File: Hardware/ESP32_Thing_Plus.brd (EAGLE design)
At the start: 22.9 x 58.4 mm, 104 parts, among them Q1 2.5A/30V, Q2 MBT3904DW1T1, U1 MCP73831, U2 ESP-WROOM-32NARROW, U3 AP2112K-3.3V, U4 CP2102N

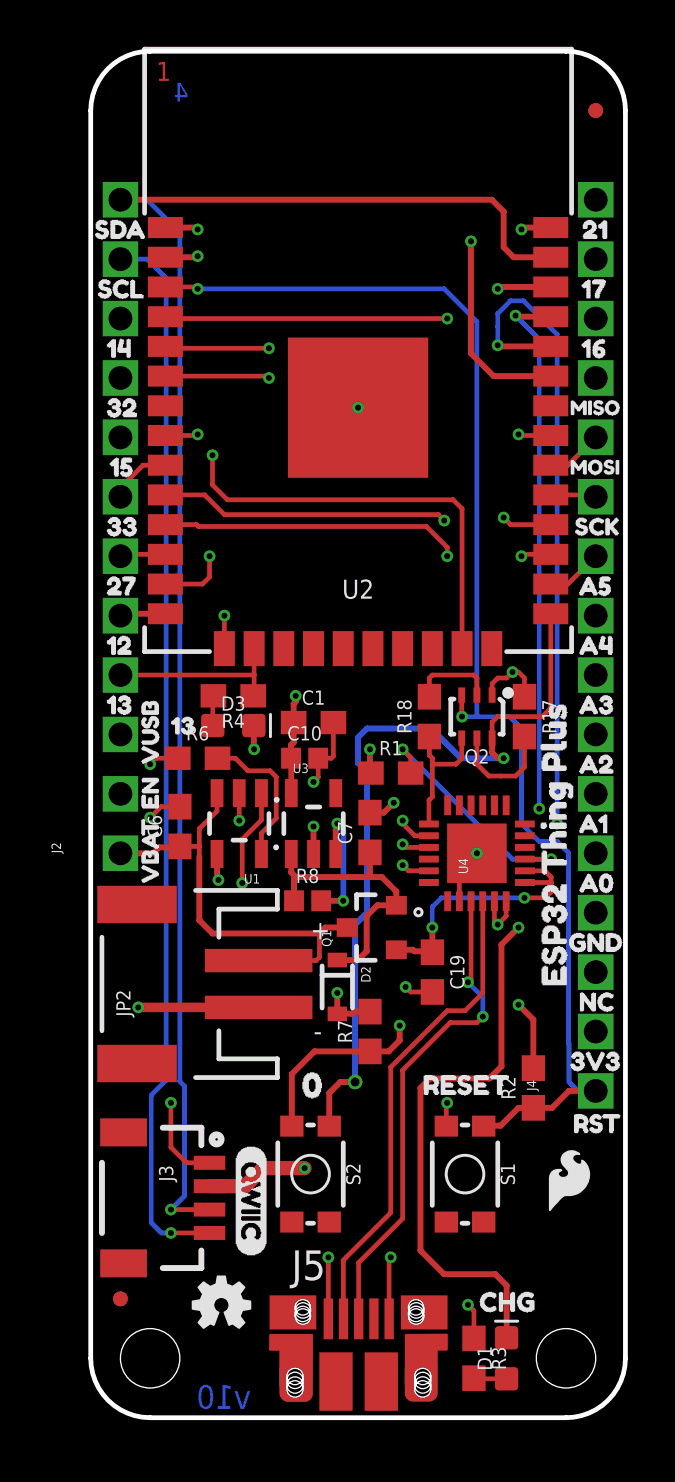
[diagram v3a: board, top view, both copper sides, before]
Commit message: v10 design review changes
- Moved battery connector away from headers by 0.030"
- Moved charge led and resistor away from standoff
- Fixed silk on header pins 21 and 12
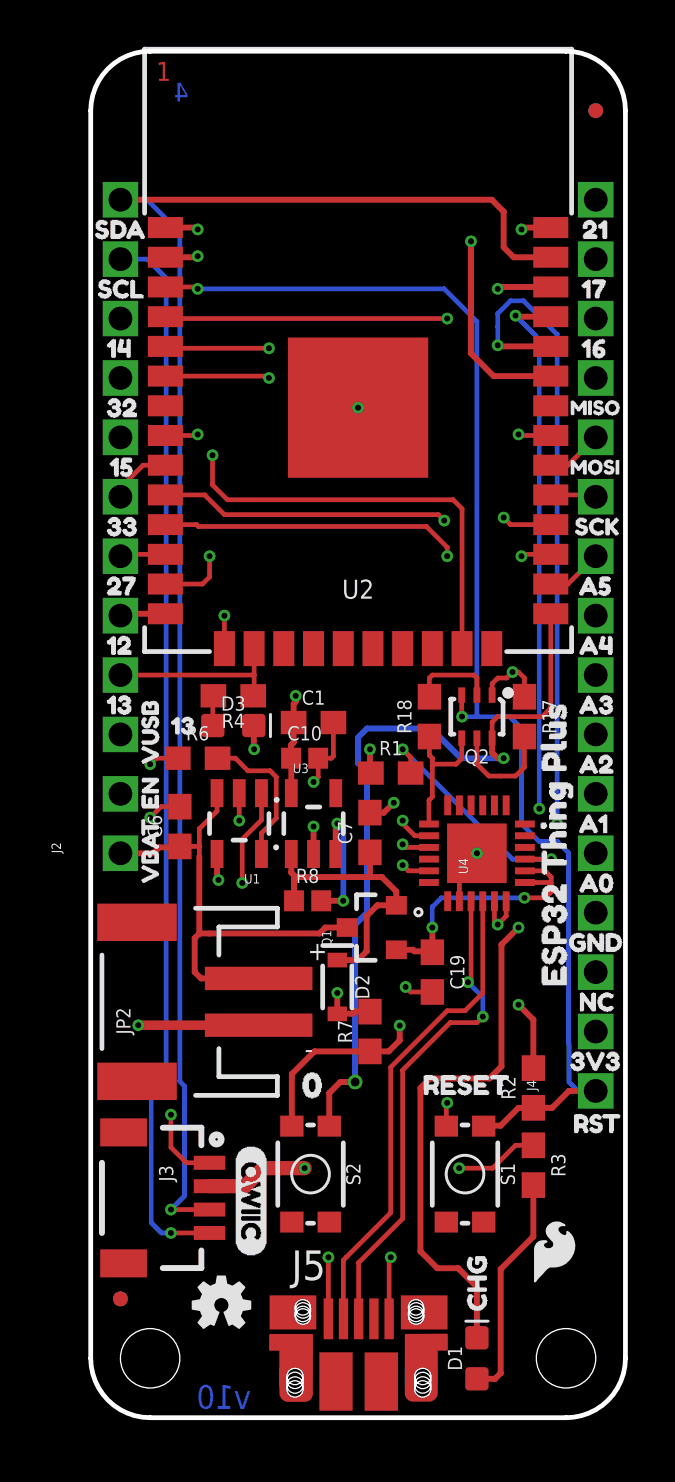
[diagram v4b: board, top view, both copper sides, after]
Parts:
- D2: value BAT20J -> 1A/23V/620mV
- Q1: device SparkFun-DiscreteSemi:SOT23-3 -> SparkFun-DiscreteSemi:SOT23-3@1
- U$8: device buzzard_labels (37):2022 -> buzzard_labels (8):121
- U$9: device buzzard_labels (37):2314 -> buzzard_labels (8):210
- moved R3 8.64 mm to (18.9, 10.8)
- moved LOGO1 3.11 mm to (18.7, 5.46)
- moved U$56 1.31 mm to (16.5, 3.81), turned to 90 degrees
- moved D1 1.27 mm to (16.5, 2.54)
- moved JP2 0.76 mm to (3.48, 17.8)
- moved U$8 0.28 mm to (4.93, 34.3)
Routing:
- net N$17: track 1.45 -> 9.74 mm
- net V_USB: track 19.5 -> 21.6 mm
- net CHG: track 41.7 -> 40.4 mm
- net V_BATT: track 19.6 -> 20.8 mm
- net GND: track 39.0 -> 38.5 mm

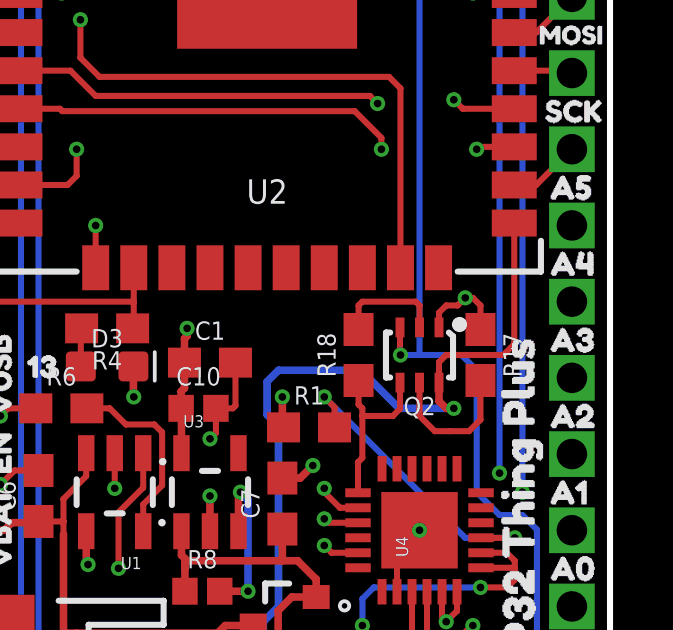
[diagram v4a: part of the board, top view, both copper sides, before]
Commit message: v10 design review changes cont.
Fixed pin 1 marker on dual NPN transistor
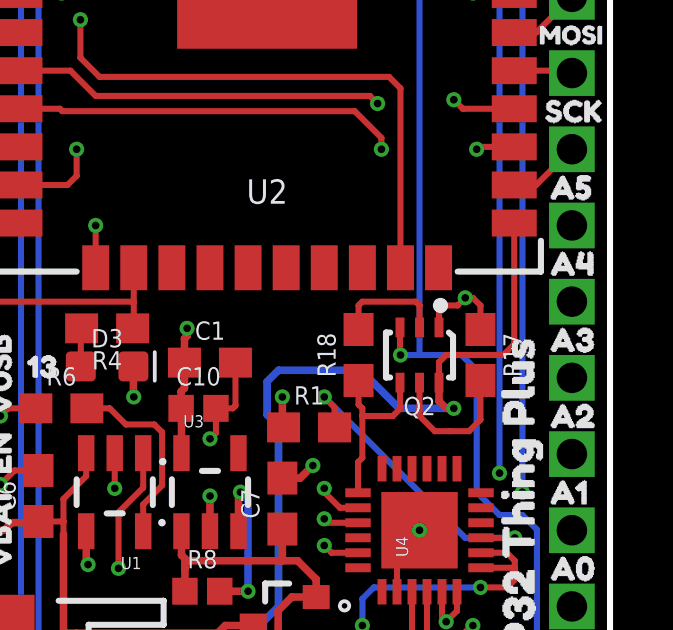
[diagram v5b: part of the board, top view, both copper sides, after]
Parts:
- Q2: device esp32-thing-temp:SC70-6 -> SparkFun-DiscreteSemi:SC70-6
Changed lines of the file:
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@@
 <attribute name="PROD_ID" value="RES-00824" x="8.128" y="18.542" size="1.778" layer="27" font="vector" ratio="15" rot="R90" display="off"/>
 </element>
-<element name="Q2" library="esp32-thing-temp" package="SC70-6" value="MBT3904DW1T1" x="16.51" y="29.972" rot="R180">
+<element name="Q2" library="SparkFun-DiscreteSemi" package="SC70-6" value="MBT3904DW1T1" x="16.51" y="29.972" rot="R180">
 <attribute name="PROD_ID" value="TRANS-13337" x="16.51" y="29.972" size="1.778" layer="27" rot="R180" display="off"/>
 </element>

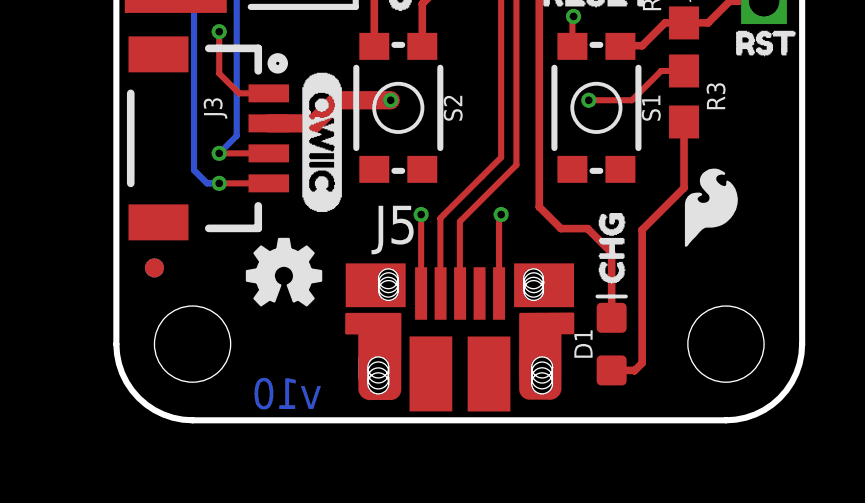
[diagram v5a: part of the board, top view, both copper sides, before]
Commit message: v10 QC Fixes
- Replaced drill hit with standoff
- Added VCC range and battery type to schematic
- Updated USB connector
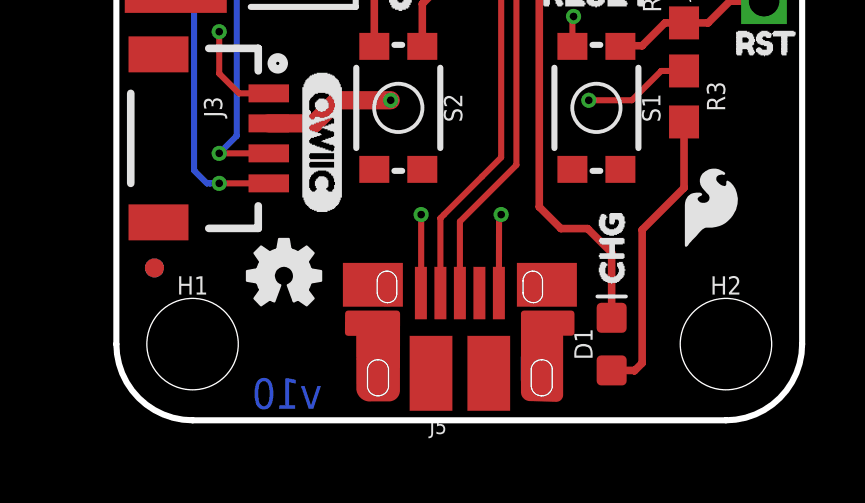
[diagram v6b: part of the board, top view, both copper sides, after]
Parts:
- added H1, H2: STAND-OFFTIGHT, SparkFun-Hardware:STAND-OFF-TIGHT
- J5: device SparkFun-Connectors:USB-MICROB-PTH -> SparkFun-Connectors:USB-MICROB-PTH-MILL
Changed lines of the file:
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@@
 <layer number="27" name="tValues" color="7" fill="1" visible="no" active="yes"/>
 <layer number="28" name="bValues" color="7" fill="1" visible="no" active="yes"/>
-<layer number="29" name="tStop" color="7" fill="3" visible="yes" active="yes"/>
+<layer number="29" name="tStop" color="7" fill="3" visible="no" active="yes"/>
 <layer number="30" name="bStop" color="7" fill="6" visible="no" active="yes"/>
 <layer number="31" name="tCream" color="7" fill="4" visible="no" active="yes"/>
@@
 <wire x1="2.54" y1="0" x2="20.32" y2="0" width="0.2032" layer="20"/>
 <wire x1="20.32" y1="0" x2="22.86" y2="2.54" width="0.2032" layer="20" curve="90"/>
-<hole x="20.32" y="2.54" drill="2.54"/>
-<hole x="2.54" y="2.54" drill="2.54"/>
 <text x="6.858" y="0.889" size="1.016" layer="16" font="vector" ratio="20" rot="MR0" align="center-left">v10</text>
 <text x="2.794" y="57.15" size="0.8128" layer="1" font="vector" ratio="25">1</text>
@@
 <element name="U$65" library="buzzard_labels" package="ESP32_THING_PLUS0" value="" x="11.43" y="43.18" rot="MR270"/>
 <element name="TP1" library="SparkFun-Connectors" package="TP_15TH" value="" x="11.303" y="14.351"/>
-<element name="J5" library="SparkFun-Connectors" package="USB-MICROB-PTH" value="" x="11.451" y="4.2418"/>
+<element name="J5" library="SparkFun-Connectors" package="USB-MICROB-PTH-MILL" value="" x="11.451" y="4.2418">
+<attribute name="PROD_ID" value="CONN-13711" x="11.451" y="4.2418" size="1.778" layer="27" display="off"/>
+</element>
 <element name="U$29" library="buzzard_labels (4)" package="SDA1" value="" x="-0.508" y="50.8"/>
 <element name="U$30" library="buzzard_labels (4)" package="SCL0" value="" x="-0.381" y="48.26"/>
@@
 <element name="U$8" library="buzzard_labels (8)" package="121" value="" x="4.9276" y="34.29" rot="MR0"/>
 <element name="U$9" library="buzzard_labels (8)" package="210" value="" x="21.1836" y="52.07" rot="MR0"/>
+<element name="H1" library="SparkFun-Hardware" package="STAND-OFF-TIGHT" value="STAND-OFFTIGHT" x="2.54" y="2.54"/>
+<element name="H2" library="SparkFun-Hardware" package="STAND-OFF-TIGHT" value="STAND-OFFTIGHT" x="20.32" y="2.54"/>
 </elements>
 <signals>
@@
 <wire x1="7.1798" y1="16.78" x2="2.032" y2="16.78" width="0.4064" layer="1"/>
 <contactref element="J5" pad="GND"/>
-<wire x1="12.75701875" y1="4.22651875" x2="12.75701875" y2="6.78801875" width="0.2032" layer="1"/>
+<wire x1="12.751" y1="4.2418" x2="12.75701875" y2="6.78801875" width="0.2032" layer="1"/>
 <wire x1="12.75701875" y1="6.78801875" x2="12.827" y2="6.858" width="0.2032" layer="1"/>
 <wire x1="9.724" y1="28.194" x2="10.287" y2="28.194" width="0.2032" layer="1"/>
@@
 <contactref element="J5" pad="VBUS"/>
 <wire x1="10.16" y1="6.858" x2="10.16" y2="4.2295" width="0.2032" layer="1"/>
-<wire x1="10.16" y1="4.2295" x2="10.15701875" y2="4.22651875" width="0.2032" layer="1"/>
+<wire x1="10.16" y1="4.2295" x2="10.151" y2="4.2418" width="0.2032" layer="1"/>
 <wire x1="18.161" y1="11.645" x2="17.184" y2="10.668" width="0.2032" layer="1"/>
 <wire x1="18.923" y1="11.645" x2="18.161" y2="11.645" width="0.2032" layer="1"/>
@@
 <wire x1="10.922" y1="6.858" x2="10.801" y2="6.737" width="0.2032" layer="1"/>
 <wire x1="10.801" y1="6.737" x2="10.801" y2="4.2325375" width="0.2032" layer="1"/>
-<wire x1="10.801" y1="4.2325375" x2="10.80701875" y2="4.22651875" width="0.2032" layer="1"/>
+<wire x1="10.801" y1="4.2325375" x2="10.801" y2="4.2418" width="0.2032" layer="1"/>
 </signal>
 <signal name="D+">
@@
 <contactref element="J5" pad="D+"/>
 <wire x1="11.451" y1="6.625" x2="11.451" y2="4.2325375" width="0.2032" layer="1"/>
-<wire x1="11.451" y1="4.2325375" x2="11.45701875" y2="4.22651875" width="0.2032" layer="1"/>
+<wire x1="11.451" y1="4.2325375" x2="11.451" y2="4.2418" width="0.2032" layer="1"/>
 </signal>
 <signal name="VIN">

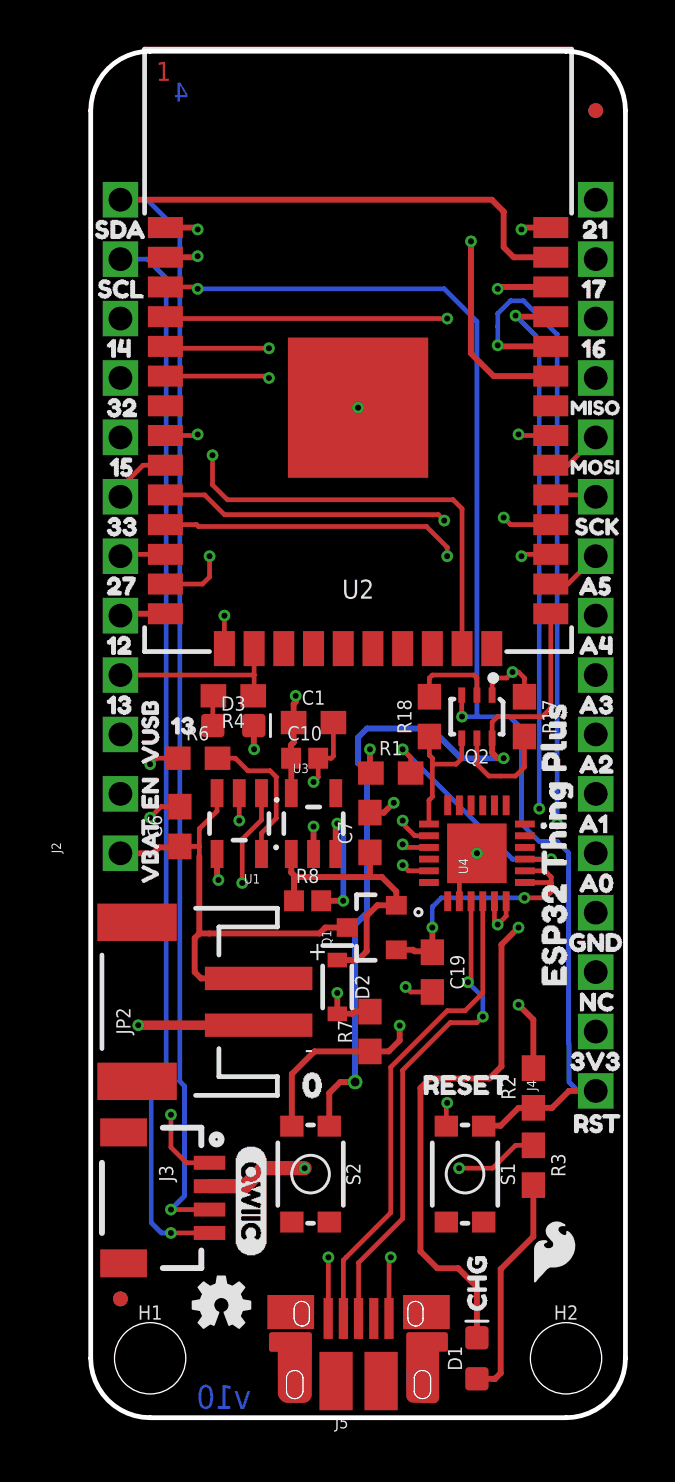
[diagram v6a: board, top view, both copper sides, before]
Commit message: v20
Added 10ohm series resistor between VUSB and CP2102
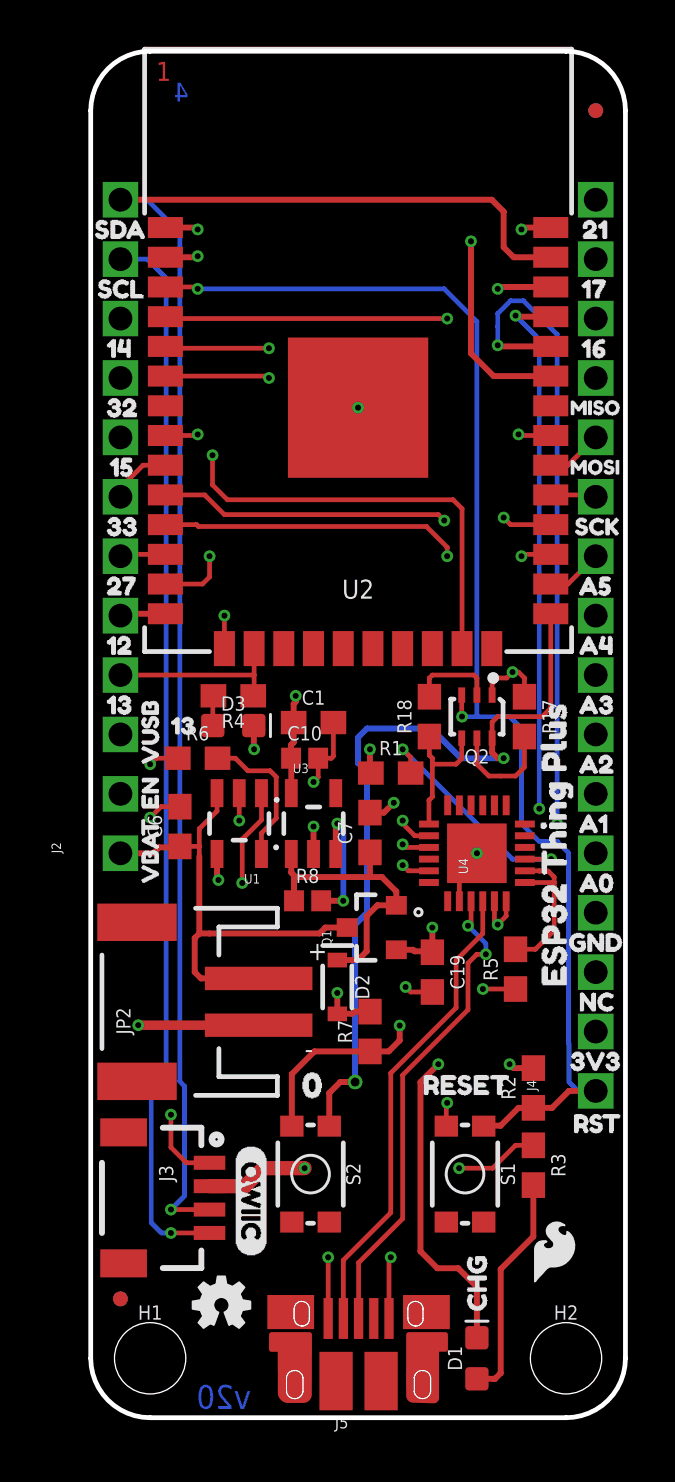
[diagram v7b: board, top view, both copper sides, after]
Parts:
- added R5: 10, SparkFun-Resistors:0603
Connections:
- removed net 2: U2.24
- removed net 35: U2.7
- new net N$3: R5.2, U4.7, U4.8
- net V_USB: now also R5.1; no longer U4.7, U4.8
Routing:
- net CHG: track 40.4 -> 31.6 mm
- net V_USB: track 21.6 -> 13.7 mm
- net N$3: track 0.00 -> 6.89 mm
- net 3.3V: track 25.9 -> 24.0 mm
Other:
- board text added: "v20"
- board text removed: "v10"

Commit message: Update ESP32_Thing_Plus.brd
Updated Buzzard Labels
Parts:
- removed U$68: (no value), buzzard_labels (6):SCL#220
- removed U$69: (no value), buzzard_labels (6):SDA#231
- added U$21: (no value), buzzard_labels (14):22#SCL1
- added U$22: (no value), buzzard_labels (14):23#SDA0
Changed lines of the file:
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@@
 <element name="U$66" library="buzzard_labels (5)" package="18#MOSI1" value="" x="21.209" y="41.91" smashed="yes" rot="MR0"/>
 <element name="U$67" library="buzzard_labels (5)" package="19#MISO0" value="" x="21.209" y="44.45" smashed="yes" rot="MR0"/>
-<element name="U$68" library="buzzard_labels (6)" package="SCL#220" value="" x="8.636" y="49.53" smashed="yes" rot="MR0"/>
-<element name="U$69" library="buzzard_labels (6)" package="SDA#231" value="" x="8.8646" y="52.07" smashed="yes" rot="MR0"/>
 <element name="U$6" library="buzzard_labels (7)" package="16#RX11" value="" x="21.209" y="46.99" smashed="yes" rot="MR0"/>
 <element name="U$7" library="buzzard_labels (7)" package="17#TX10" value="" x="21.209" y="49.53" smashed="yes" rot="MR0"/>
@@
 <attribute name="VALUE" x="18.923" y="19.177" size="0.6096" layer="27" font="vector" ratio="20" rot="R90" align="top-center"/>
 </element>
+<element name="U$21" library="buzzard_labels (14)" package="22#SCL1" value="" x="8.636" y="49.53" smashed="yes" rot="MR0"/>
+<element name="U$22" library="buzzard_labels (14)" package="23#SDA0" value="" x="8.8646" y="52.07" smashed="yes" rot="MR0"/>
 </elements>
 <signals>
